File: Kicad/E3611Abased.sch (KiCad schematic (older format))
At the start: 1 part, among them J1 Conn_02x05_Odd_Even

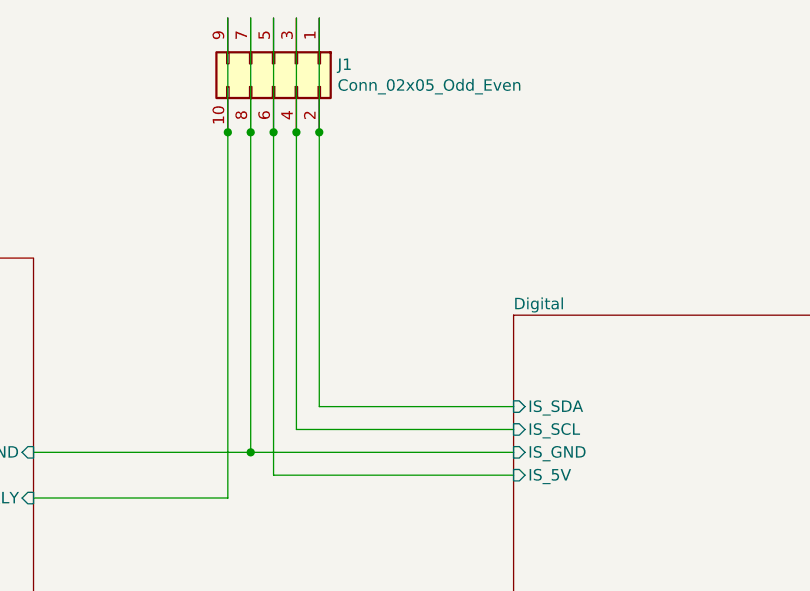
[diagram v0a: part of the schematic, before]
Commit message: fixed bugs in PCB, added frontpanel, added SW for frontpanel
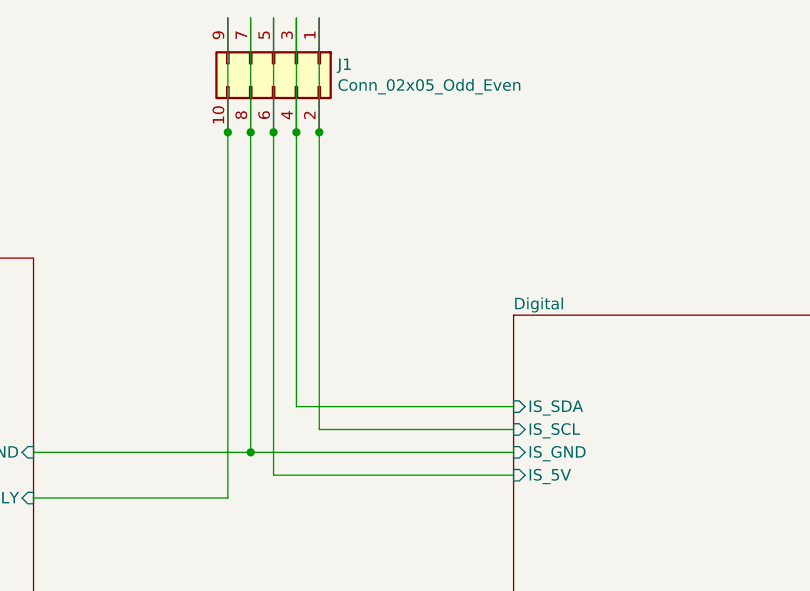
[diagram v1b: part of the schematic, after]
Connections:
- net Digital/IS_SCL: now also J1.1 (Pin_1), J1.2 (Pin_2); no longer J1.3 (Pin_3), J1.4 (Pin_4)
- net Digital/IS_SDA: now also J1.3 (Pin_3), J1.4 (Pin_4); no longer J1.1 (Pin_1), J1.2 (Pin_2)
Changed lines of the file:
@@
 	5700 2900 5700 3400
 Wire Wire Line
-	5700 3400 5700 4700
+	5700 3400 5700 4600
 Wire Wire Line
-	5700 4700 6650 4700
+	5700 4600 6650 4600
 Connection ~ 5700 3400
 Wire Wire Line
-	6650 4600 5800 4600
+	5800 4700 5800 3400
 Wire Wire Line
-	5800 4600 5800 3400
+	5800 4700 6650 4700
 Wire Wire Line
 	5800 3400 5800 2900
